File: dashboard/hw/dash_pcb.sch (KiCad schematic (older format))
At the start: 35 parts, among them J1 LCD, J2 DEBUG, J3 LCD_BL, J4 CAR, U1 LPC11C24FBD48, U2 TPS62175, U3 TLV70233_SOT23-5, Y1 12MHz

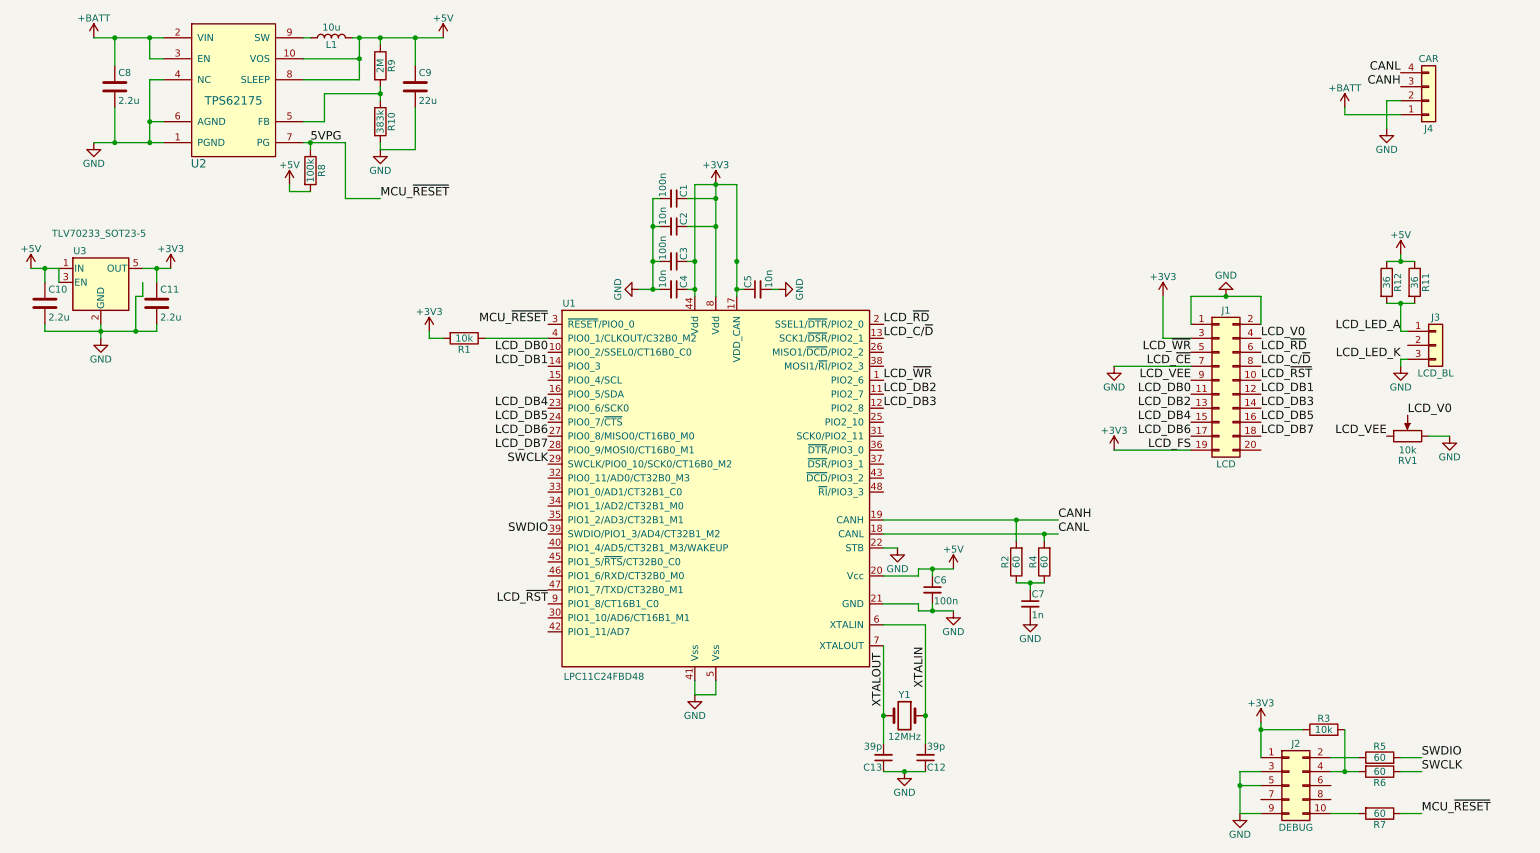
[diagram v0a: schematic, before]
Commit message: add jumpers to selectively terminate can bus
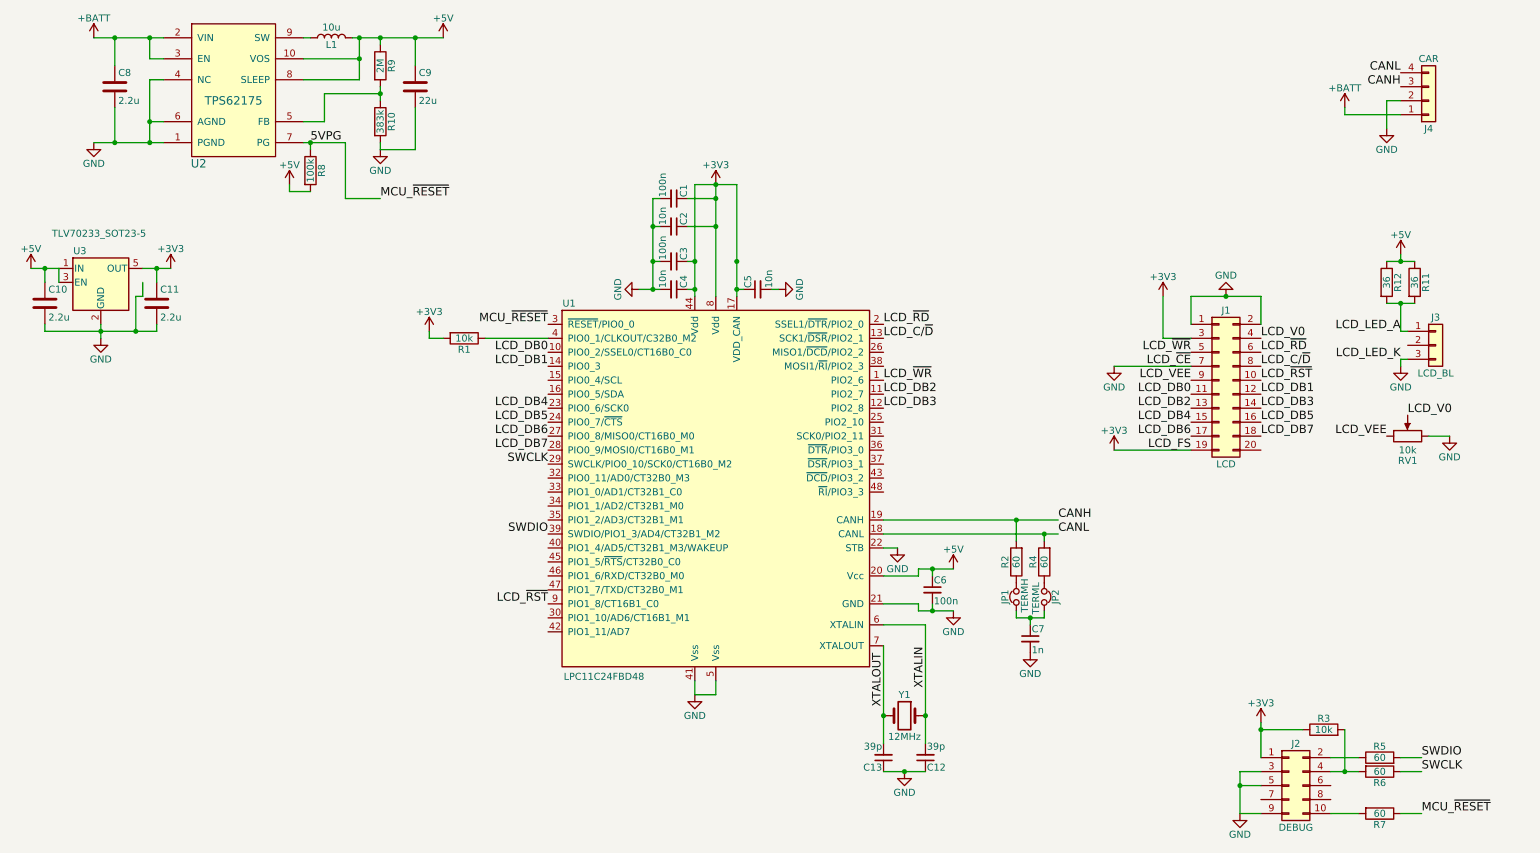
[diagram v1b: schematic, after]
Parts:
- added JP1: TERMH, Pin_Headers:Pin_Header_Angled_1x02_Pitch2.54mm, symbol Jumper_NC_Small
- added JP2: TERML, Pin_Headers:Pin_Header_Angled_1x02_Pitch2.54mm, symbol Jumper_NC_Small
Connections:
- new net: JP1.2, R2.1
- new net: JP2.1, R4.1
- new net: C7.1, JP1.1, JP2.2
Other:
- moved on the sheet: C7
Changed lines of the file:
@@
 L C_Small C7
 U 1 1 5AED813D
-P 7850 4800
-F 0 "C7" H 7860 4870 50  0000 L CNN
-F 1 "1n" H 7860 4720 50  0000 L CNN
-F 2 "Capacitors_SMD:C_0603" H 7850 4800 50  0001 C CNN
-F 3 "" H 7850 4800 50  0001 C CNN
-	1    7850 4800
+P 7850 5050
+F 0 "C7" H 7860 5120 50  0000 L CNN
+F 1 "1n" H 7860 4970 50  0000 L CNN
+F 2 "Capacitors_SMD:C_0603" H 7850 5050 50  0001 C CNN
+F 3 "" H 7850 5050 50  0001 C CNN
+	1    7850 5050
 	1    0    0    -1
 $EndComp
@@
 L GND #PWR012
 U 1 1 5AED81B0
-P 7850 4900
-F 0 "#PWR012" H 7850 4650 50  0001 C CNN
-F 1 "GND" H 7850 4750 50  0000 C CNN
-F 2 "" H 7850 4900 50  0001 C CNN
-F 3 "" H 7850 4900 50  0001 C CNN
-	1    7850 4900
+P 7850 5150
+F 0 "#PWR012" H 7850 4900 50  0001 C CNN
+F 1 "GND" H 7850 5000 50  0000 C CNN
+F 2 "" H 7850 5150 50  0001 C CNN
+F 3 "" H 7850 5150 50  0001 C CNN
+	1    7850 5150
 	1    0    0    -1
 $EndComp
@@
 Connection ~ 7950 4300
 Wire Wire Line
-	7750 4650 7950 4650
-Wire Wire Line
-	7850 4650 7850 4700
-Connection ~ 7850 4650
-Wire Wire Line
 	10650 6300 10500 6300
 Wire Wire Line
@@
 	1650 900  1550 900
 Wire Wire Line
-	1550 750  1550 900
+	1550 900  1550 750
 Connection ~ 1550 750
 Wire Wire Line
@@
 Wire Wire Line
 	1500 2600 1500 2500
+$Comp
+L Jumper_NC_Small JP1
+U 1 1 5AFBFB6B
+P 7750 4750
+F 0 "JP1" H 7750 4830 50  0000 C CNN
+F 1 "TERMH" H 7760 4690 50  0000 C CNN
+F 2 "Pin_Headers:Pin_Header_Angled_1x02_Pitch2.54mm" H 7750 4750 50  0001 C CNN
+F 3 "" H 7750 4750 50  0001 C CNN
+	1    7750 4750
+	0    -1   -1   0
+$EndComp
+$Comp
+L Jumper_NC_Small JP2
+U 1 1 5AFBFC52
+P 7950 4750
+F 0 "JP2" H 7950 4830 50  0000 C CNN
+F 1 "TERML" H 7960 4690 50  0000 C CNN
+F 2 "Pin_Headers:Pin_Header_Angled_1x02_Pitch2.54mm" H 7950 4750 50  0001 C CNN
+F 3 "" H 7950 4750 50  0001 C CNN
+	1    7950 4750
+	0    1    1    0
+$EndComp
+Wire Wire Line
+	7750 4850 7750 4900
+Wire Wire Line
+	7750 4900 7950 4900
+Wire Wire Line
+	7950 4900 7950 4850
+Wire Wire Line
+	7850 4900 7850 4950
+Connection ~ 7850 4900
 $EndSCHEMATC

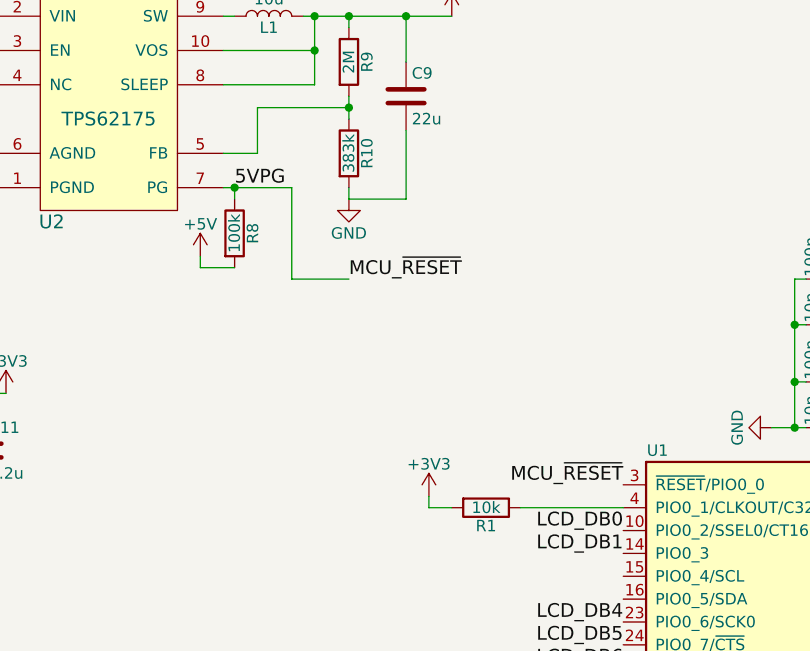
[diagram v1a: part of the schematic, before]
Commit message: pull reset to 3.3 instead of 5
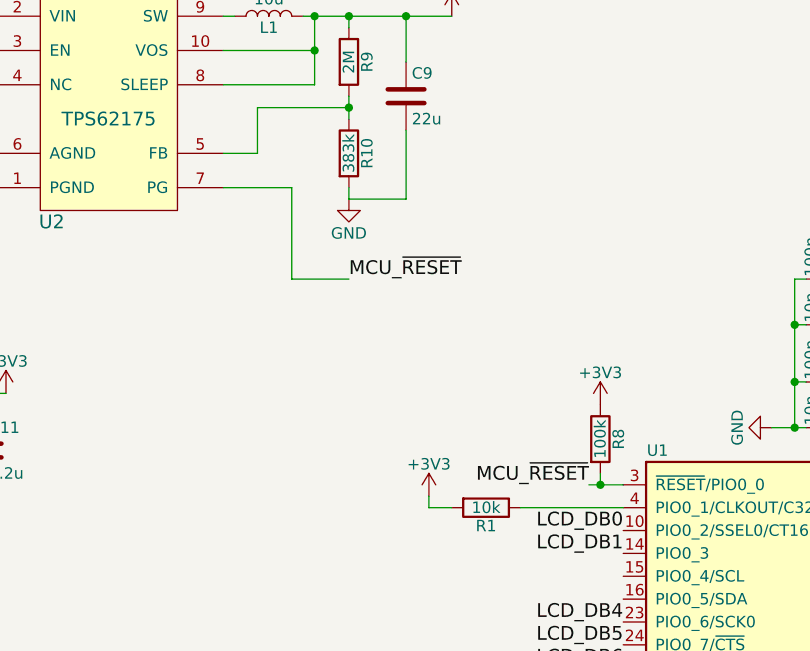
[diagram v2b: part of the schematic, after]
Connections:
- net +3V3: now also R8.1
- net +5V: no longer R8.2
- net 5VPG renamed MCU_~RESET
- net MCU_~RESET: now also R8.2; no longer R8.1
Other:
- moved on the sheet: R8
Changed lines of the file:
@@
 Text Label 4400 4300 2    60   ~ 0
 SWDIO
-Text Label 4400 2800 2    60   ~ 0
+Text Label 4250 2800 2    60   ~ 0
 MCU_~RESET
 $Comp
@@
 	1    0    0    -1
 $EndComp
-Text Label 2700 1500 0    60   ~ 0
-5VPG
 $Comp
 L TPS62175 U2
@@
 L R R8
 U 1 1 5AF015E3
-P 2700 1700
-F 0 "R8" V 2780 1700 50  0000 C CNN
-F 1 "100k" V 2700 1700 50  0000 C CNN
-F 2 "Resistors_SMD:R_0603" V 2630 1700 50  0001 C CNN
-F 3 "" H 2700 1700 50  0001 C CNN
-	1    2700 1700
-	1    0    0    -1
-$EndComp
-$Comp
-L +5V #PWR018
-U 1 1 5AF017BC
-P 2550 1800
-F 0 "#PWR018" H 2550 1650 50  0001 C CNN
-F 1 "+5V" H 2550 1940 50  0000 C CNN
-F 2 "" H 2550 1800 50  0001 C CNN
-F 3 "" H 2550 1800 50  0001 C CNN
-	1    2550 1800
+P 4300 2600
+F 0 "R8" V 4380 2600 50  0000 C CNN
+F 1 "100k" V 4300 2600 50  0000 C CNN
+F 2 "Resistors_SMD:R_0603" V 4230 2600 50  0001 C CNN
+F 3 "" H 4300 2600 50  0001 C CNN
+	1    4300 2600
 	1    0    0    -1
 $EndComp
@@
 	2650 1500 2950 1500
 Wire Wire Line
-	2700 1500 2700 1550
-Wire Wire Line
-	2550 1800 2550 1850
-Wire Wire Line
-	2550 1850 2700 1850
-Wire Wire Line
 	2650 750  2700 750
 Wire Wire Line
@@
 Wire Wire Line
 	2950 1900 3200 1900
-Connection ~ 2700 1500
 Wire Wire Line
 	1500 2600 1450 2600
@@
 	7850 4900 7850 4950
 Connection ~ 7850 4900
+Wire Wire Line
+	4250 2800 4400 2800
+Connection ~ 4300 2800
+$Comp
+L +3V3 #PWR?
+U 1 1 5AFC1DF1
+P 4300 2450
+F 0 "#PWR?" H 4300 2300 50  0001 C CNN
+F 1 "+3V3" H 4300 2590 50  0000 C CNN
+F 2 "" H 4300 2450 50  0001 C CNN
+F 3 "" H 4300 2450 50  0001 C CNN
+	1    4300 2450
+	1    0    0    -1
+$EndComp
+Wire Wire Line
+	4300 2750 4300 2800
 $EndSCHEMATC

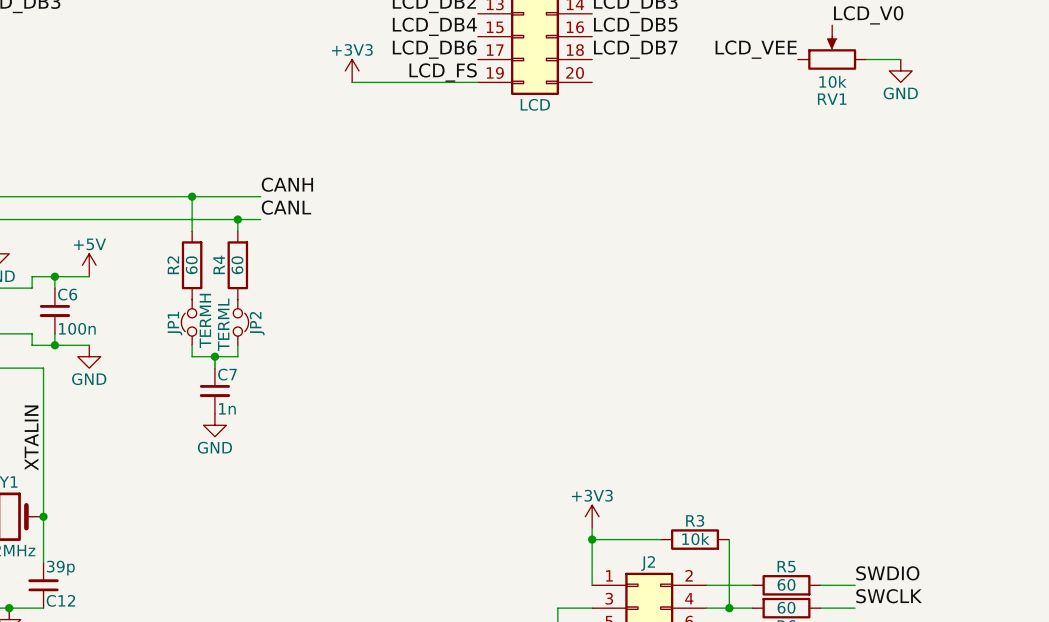
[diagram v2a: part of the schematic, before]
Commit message: change termination jumpers to dip switches
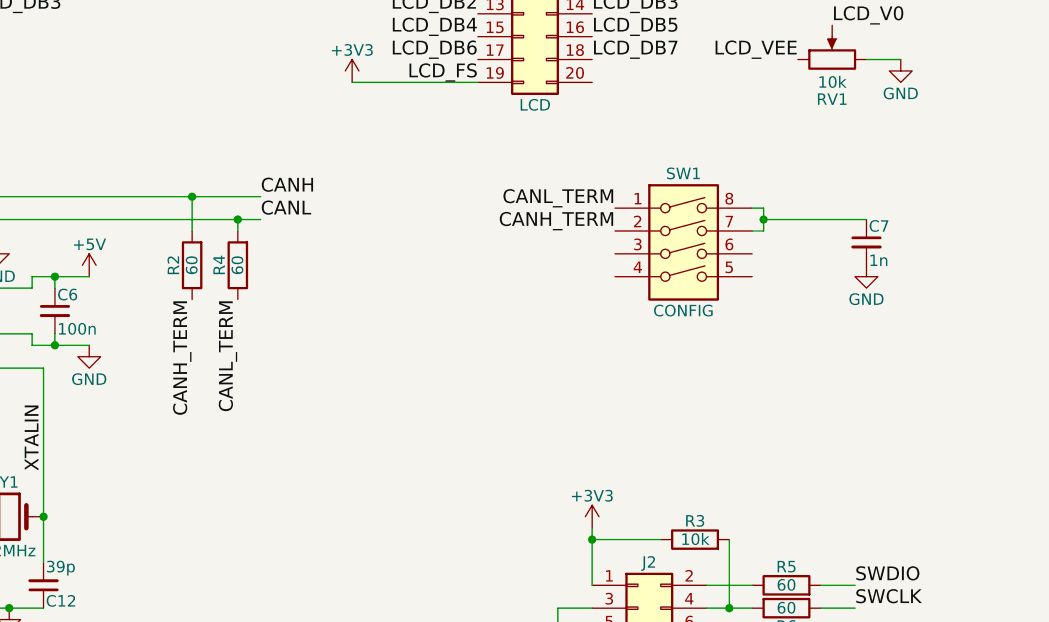
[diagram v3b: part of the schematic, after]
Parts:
- removed JP1: TERMH, Pin_Headers:Pin_Header_Angled_1x02_Pitch2.54mm, symbol Jumper_NC_Small
- removed JP2: TERML, Pin_Headers:Pin_Header_Angled_1x02_Pitch2.54mm, symbol Jumper_NC_Small
- added SW1: CONFIG, Buttons_Switches_THT:SW_DIP_x4_W7.62mm_Slide, symbol SW_DIP_x04
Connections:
- net CANH_TERM: now reaches R2.1
- net CANH_TERM: now also SW1.2
- net CANL_TERM: now reaches R4.1
- net CANL_TERM: now also SW1.1
- net at C7.1: now also SW1.7, SW1.8
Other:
- moved on the sheet: C7
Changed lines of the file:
@@
 LIBS:lmz21700
 LIBS:tps6217x
+LIBS:switches
 LIBS:dash_pcb-cache
 EELAYER 25 0
@@
 L C_Small C7
 U 1 1 5AED813D
-P 7850 5050
-F 0 "C7" H 7860 5120 50  0000 L CNN
-F 1 "1n" H 7860 4970 50  0000 L CNN
-F 2 "Capacitors_SMD:C_0603" H 7850 5050 50  0001 C CNN
-F 3 "" H 7850 5050 50  0001 C CNN
-	1    7850 5050
+P 10700 4400
+F 0 "C7" H 10710 4470 50  0000 L CNN
+F 1 "1n" H 10710 4320 50  0000 L CNN
+F 2 "Capacitors_SMD:C_0603" H 10700 4400 50  0001 C CNN
+F 3 "" H 10700 4400 50  0001 C CNN
+	1    10700 4400
 	1    0    0    -1
 $EndComp
@@
 L GND #PWR012
 U 1 1 5AED81B0
-P 7850 5150
-F 0 "#PWR012" H 7850 4900 50  0001 C CNN
-F 1 "GND" H 7850 5000 50  0000 C CNN
-F 2 "" H 7850 5150 50  0001 C CNN
-F 3 "" H 7850 5150 50  0001 C CNN
-	1    7850 5150
+P 10700 4500
+F 0 "#PWR012" H 10700 4250 50  0001 C CNN
+F 1 "GND" H 10700 4350 50  0000 C CNN
+F 2 "" H 10700 4500 50  0001 C CNN
+F 3 "" H 10700 4500 50  0001 C CNN
+	1    10700 4500
 	1    0    0    -1
 $EndComp
@@
 $EndComp
 $Comp
-L +5V #PWR019
+L +5V #PWR018
 U 1 1 5AF01C77
 P 3650 750
-F 0 "#PWR019" H 3650 600 50  0001 C CNN
+F 0 "#PWR018" H 3650 600 50  0001 C CNN
 F 1 "+5V" H 3650 890 50  0000 C CNN
 F 2 "" H 3650 750 50  0001 C CNN
@@
 $EndComp
 $Comp
-L GND #PWR020
+L GND #PWR019
 U 1 1 5AF028D7
 P 3200 1550
-F 0 "#PWR020" H 3200 1300 50  0001 C CNN
+F 0 "#PWR019" H 3200 1300 50  0001 C CNN
 F 1 "GND" H 3200 1400 50  0000 C CNN
 F 2 "" H 3200 1550 50  0001 C CNN
@@
 $EndComp
 $Comp
-L GND #PWR021
+L GND #PWR020
 U 1 1 5AF0183D
 P 1200 2900
-F 0 "#PWR021" H 1200 2650 50  0001 C CNN
+F 0 "#PWR020" H 1200 2650 50  0001 C CNN
 F 1 "GND" H 1200 2750 50  0000 C CNN
 F 2 "" H 1200 2900 50  0001 C CNN
@@
 $EndComp
 $Comp
-L +5V #PWR022
+L +5V #PWR021
 U 1 1 5AF01B37
 P 700 2400
-F 0 "#PWR022" H 700 2250 50  0001 C CNN
+F 0 "#PWR021" H 700 2250 50  0001 C CNN
 F 1 "+5V" H 700 2540 50  0000 C CNN
 F 2 "" H 700 2400 50  0001 C CNN
@@
 $EndComp
 $Comp
-L +3V3 #PWR023
+L +3V3 #PWR022
 U 1 1 5AF0216E
 P 1700 2400
-F 0 "#PWR023" H 1700 2250 50  0001 C CNN
+F 0 "#PWR022" H 1700 2250 50  0001 C CNN
 F 1 "+3V3" H 1700 2540 50  0000 C CNN
 F 2 "" H 1700 2400 50  0001 C CNN
@@
 $EndComp
 $Comp
-L GND #PWR024
+L GND #PWR023
 U 1 1 5AF045C8
 P 6950 6000
-F 0 "#PWR024" H 6950 5750 50  0001 C CNN
+F 0 "#PWR023" H 6950 5750 50  0001 C CNN
 F 1 "GND" H 6950 5850 50  0000 C CNN
 F 2 "" H 6950 6000 50  0001 C CNN
@@
 XTALOUT
 $Comp
-L GND #PWR025
+L GND #PWR024
 U 1 1 5AF17E60
 P 10500 3100
-F 0 "#PWR025" H 10500 2850 50  0001 C CNN
+F 0 "#PWR024" H 10500 2850 50  0001 C CNN
 F 1 "GND" H 10500 2950 50  0000 C CNN
 F 2 "" H 10500 3100 50  0001 C CNN
@@
 $EndComp
 $Comp
-L +5V #PWR026
+L +5V #PWR025
 U 1 1 5AF1A42C
 P 10500 2300
-F 0 "#PWR026" H 10500 2150 50  0001 C CNN
+F 0 "#PWR025" H 10500 2150 50  0001 C CNN
 F 1 "+5V" H 10500 2440 50  0000 C CNN
 F 2 "" H 10500 2300 50  0001 C CNN
@@
 $EndComp
 $Comp
-L +BATT #PWR027
+L +BATT #PWR026
 U 1 1 5AF2F5B2
 P 1150 750
-F 0 "#PWR027" H 1150 600 50  0001 C CNN
+F 0 "#PWR026" H 1150 600 50  0001 C CNN
 F 1 "+BATT" H 1150 890 50  0000 C CNN
 F 2 "" H 1150 750 50  0001 C CNN
@@
 CANL
 $Comp
-L +BATT #PWR028
+L +BATT #PWR027
 U 1 1 5AF308D1
 P 10100 1250
-F 0 "#PWR028" H 10100 1100 50  0001 C CNN
+F 0 "#PWR027" H 10100 1100 50  0001 C CNN
 F 1 "+BATT" H 10100 1390 50  0000 C CNN
 F 2 "" H 10100 1250 50  0001 C CNN
@@
 $EndComp
 $Comp
-L GND #PWR029
+L GND #PWR028
 U 1 1 5AF313E9
 P 10400 1400
-F 0 "#PWR029" H 10400 1150 50  0001 C CNN
+F 0 "#PWR028" H 10400 1150 50  0001 C CNN
 F 1 "GND" H 10400 1250 50  0000 C CNN
 F 2 "" H 10400 1400 50  0001 C CNN
@@
 Wire Wire Line
 	1500 2600 1500 2500
-$Comp
-L Jumper_NC_Small JP1
-U 1 1 5AFBFB6B
-P 7750 4750
-F 0 "JP1" H 7750 4830 50  0000 C CNN
-F 1 "TERMH" H 7760 4690 50  0000 C CNN
-F 2 "Pin_Headers:Pin_Header_Angled_1x02_Pitch2.54mm" H 7750 4750 50  0001 C CNN
-F 3 "" H 7750 4750 50  0001 C CNN
-	1    7750 4750
-	0    -1   -1   0
-$EndComp
-$Comp
-L Jumper_NC_Small JP2
-U 1 1 5AFBFC52
-P 7950 4750
-F 0 "JP2" H 7950 4830 50  0000 C CNN
-F 1 "TERML" H 7960 4690 50  0000 C CNN
-F 2 "Pin_Headers:Pin_Header_Angled_1x02_Pitch2.54mm" H 7950 4750 50  0001 C CNN
-F 3 "" H 7950 4750 50  0001 C CNN
-	1    7950 4750
-	0    1    1    0
-$EndComp
-Wire Wire Line
-	7750 4850 7750 4900
-Wire Wire Line
-	7750 4900 7950 4900
-Wire Wire Line
-	7950 4900 7950 4850
-Wire Wire Line
-	7850 4900 7850 4950
-Connection ~ 7850 4900
 Wire Wire Line
 	4250 2800 4400 2800
 Connection ~ 4300 2800
 $Comp
-L +3V3 #PWR?
+L +3V3 #PWR029
 U 1 1 5AFC1DF1
 P 4300 2450
-F 0 "#PWR?" H 4300 2300 50  0001 C CNN
+F 0 "#PWR029" H 4300 2300 50  0001 C CNN
 F 1 "+3V3" H 4300 2590 50  0000 C CNN
 F 2 "" H 4300 2450 50  0001 C CNN
@@
 Wire Wire Line
 	4300 2750 4300 2800
+$Comp
+L SW_DIP_x04 SW1
+U 1 1 5AFC4E3D
+P 9900 4450
+F 0 "SW1" H 9900 4800 50  0000 C CNN
+F 1 "CONFIG" H 9900 4200 50  0000 C CNN
+F 2 "Buttons_Switches_THT:SW_DIP_x4_W7.62mm_Slide" H 9900 4450 50  0001 C CNN
+F 3 "https://www.mouser.de/ProductDetail/TE-Connectivity-Alcoswitch/ADE0404?qs=sGAEpiMZZMv%2f%252b2JhlA6ysER62VlXw6iZ4HTlb4kKXdw%3d" H 9900 4450 50  0001 C CNN
+	1    9900 4450
+	1    0    0    -1
+$EndComp
+Wire Wire Line
+	10200 4250 10250 4250
+Wire Wire Line
+	10250 4250 10250 4350
+Wire Wire Line
+	10250 4350 10200 4350
+Wire Wire Line
+	10250 4300 10700 4300
+Connection ~ 10250 4300
+Text Label 7750 4650 3    60   ~ 0
+CANH_TERM
+Text Label 7950 4650 3    60   ~ 0
+CANL_TERM
+Text Label 9600 4350 2    60   ~ 0
+CANH_TERM
+Text Label 9600 4250 2    60   ~ 0
+CANL_TERM
 $EndSCHEMATC
